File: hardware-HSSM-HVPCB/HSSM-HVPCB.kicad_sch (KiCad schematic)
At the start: 30 parts, among them J1 2086-1103, J2 2601-1110, K1 G6DN-1A-L DC12, K2 G6DN-1A-L DC12, Q1 Q_NMOS_SOT-23_IRLML6344, Q2 Q_NMOS_SOT-23_IRLML6344, U1 LNK3202D-TL, U2 CS5480-INZ

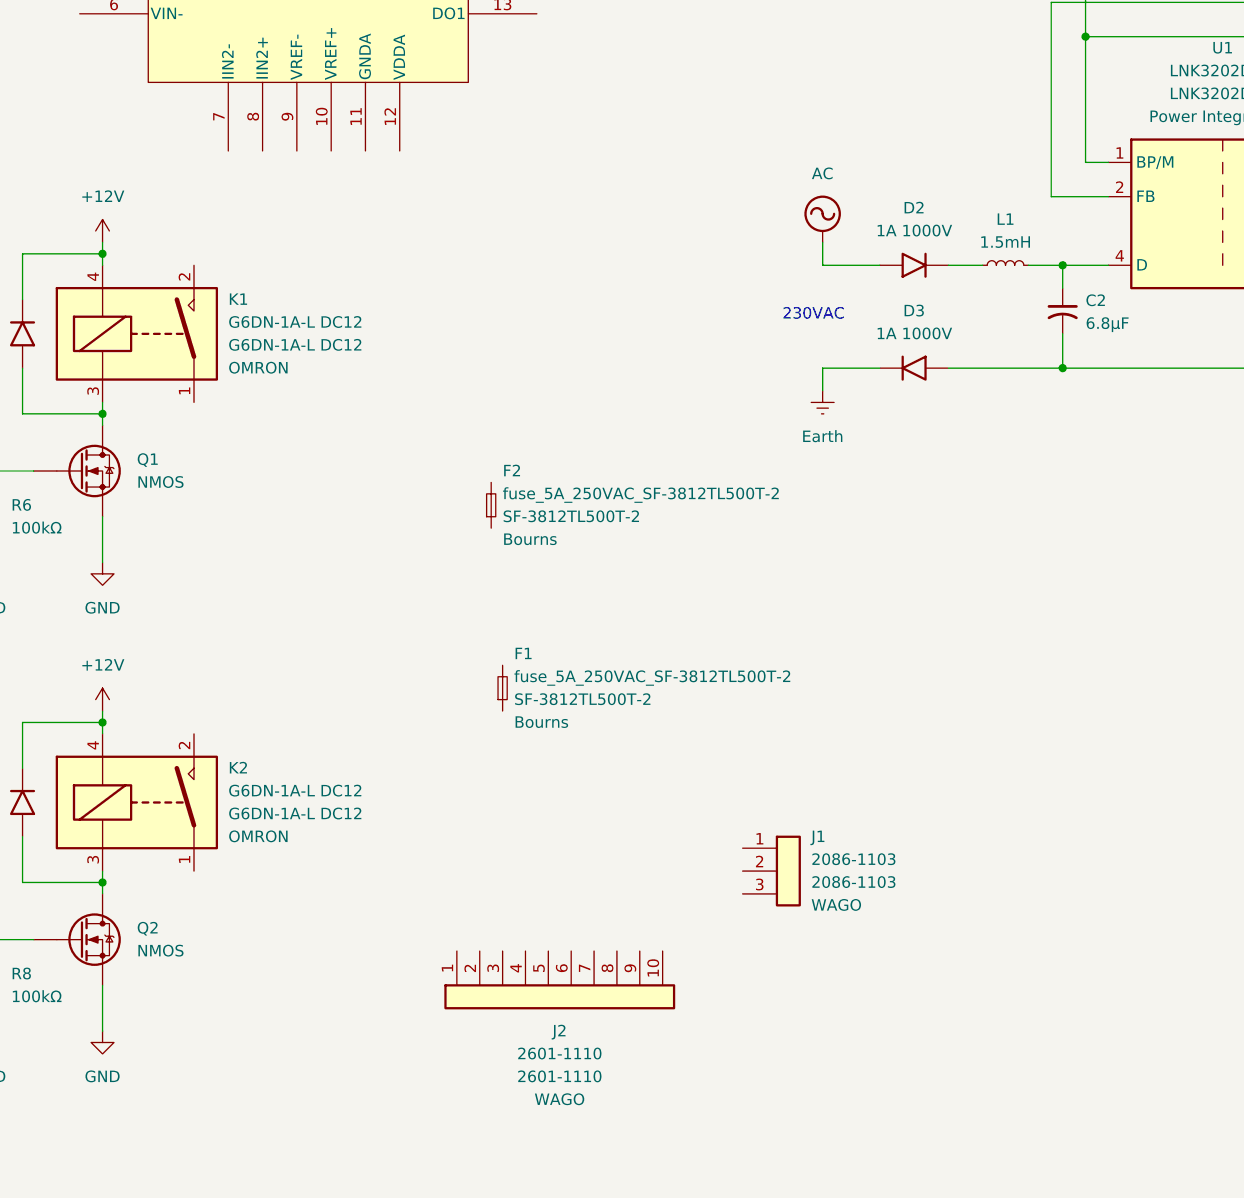
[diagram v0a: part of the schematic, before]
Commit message: [#3] SCH relay output
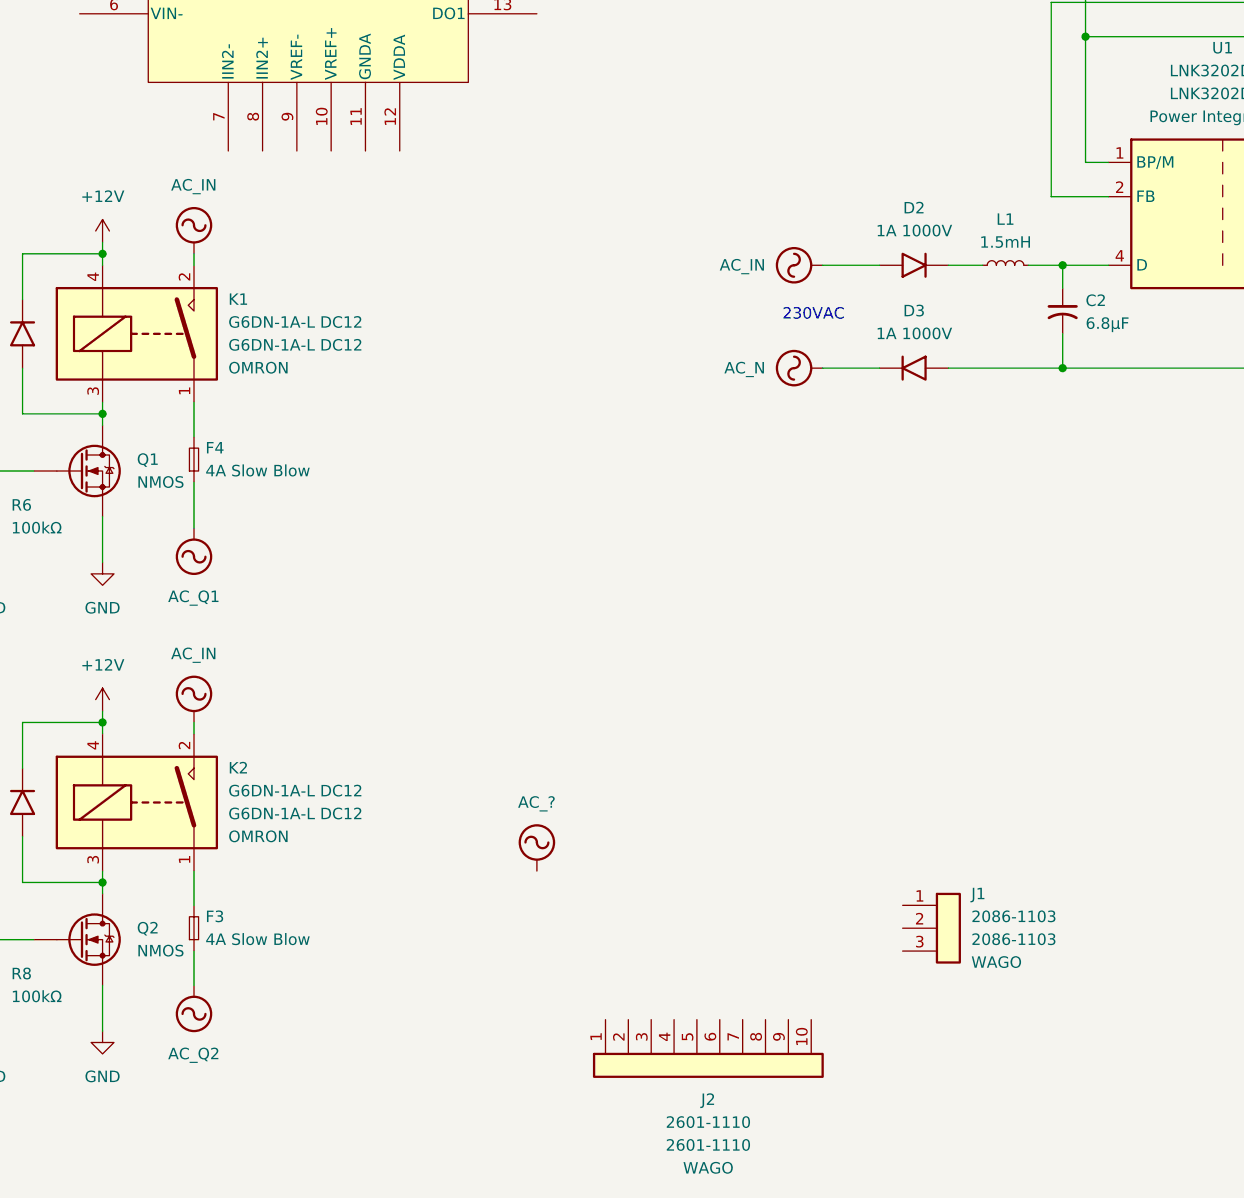
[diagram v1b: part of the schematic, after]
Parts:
- removed F1, F2: fuse_5A_250VAC_SF-3812TL500T-2, symbol HSSM-HVPCB:fuse_5A_250VAC_SF-3812TL500T-2
- added F3, F4: F_4A_SlowBlow_Holder_UMZ250_3404.2422.11, HSSM-HVPCB:F_Holder_UMZ250, symbol HSSM-HVPCB:F_4A_SlowBlow_Holder_UMZ250_3404.2422.11
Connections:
- net AC is gone; now on net AC_IN: D2.2 (A)
- net at K1.1: now also F4.2
- net AC_IN: now reaches K1.2
- net AC_IN: now also K2.2
- net at K2.1: now also F3.2
- net Earth renamed AC_N
- new net AC_Q1: F4.1
- new net AC_Q2: F3.1
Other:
- moved on the sheet: J1, J2

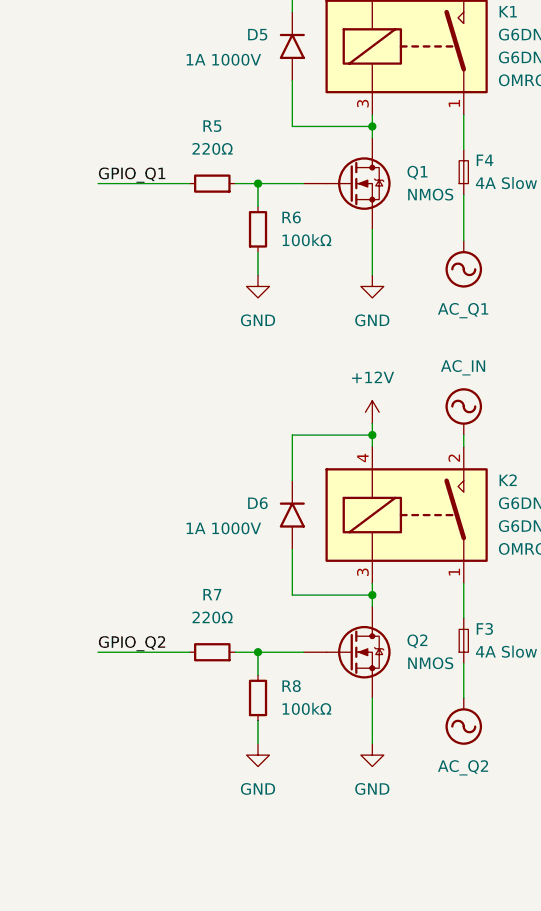
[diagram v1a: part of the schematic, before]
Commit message: [#3] SCH add relay status leds
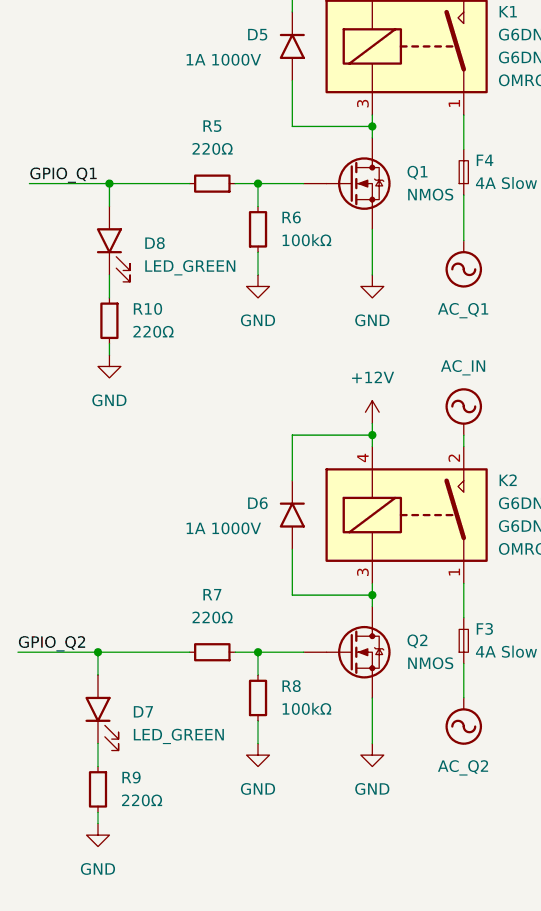
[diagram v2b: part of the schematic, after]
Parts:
- added D7, D8: LED_Green_Kingbright_APHHS1005CGCK, HSSM-HVPCB:LED_1005, symbol HSSM-HVPCB:LED_Green_Kingbright_APHHS1005CGCK
- added R10, R9: R_220R_1pct_0402_RC0402FR-07220RL, HSSM-HVPCB:R_0402, symbol HSSM-HVPCB:R_220R_1pct_0402_RC0402FR-07220RL
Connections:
- net GND: now also R10.2, R9.2
- net GPIO_Q1: now also D8.2 (A)
- net GPIO_Q2: now also D7.2 (A)
- new net: D8.1 (K), R10.1
- new net: D7.1 (K), R9.1

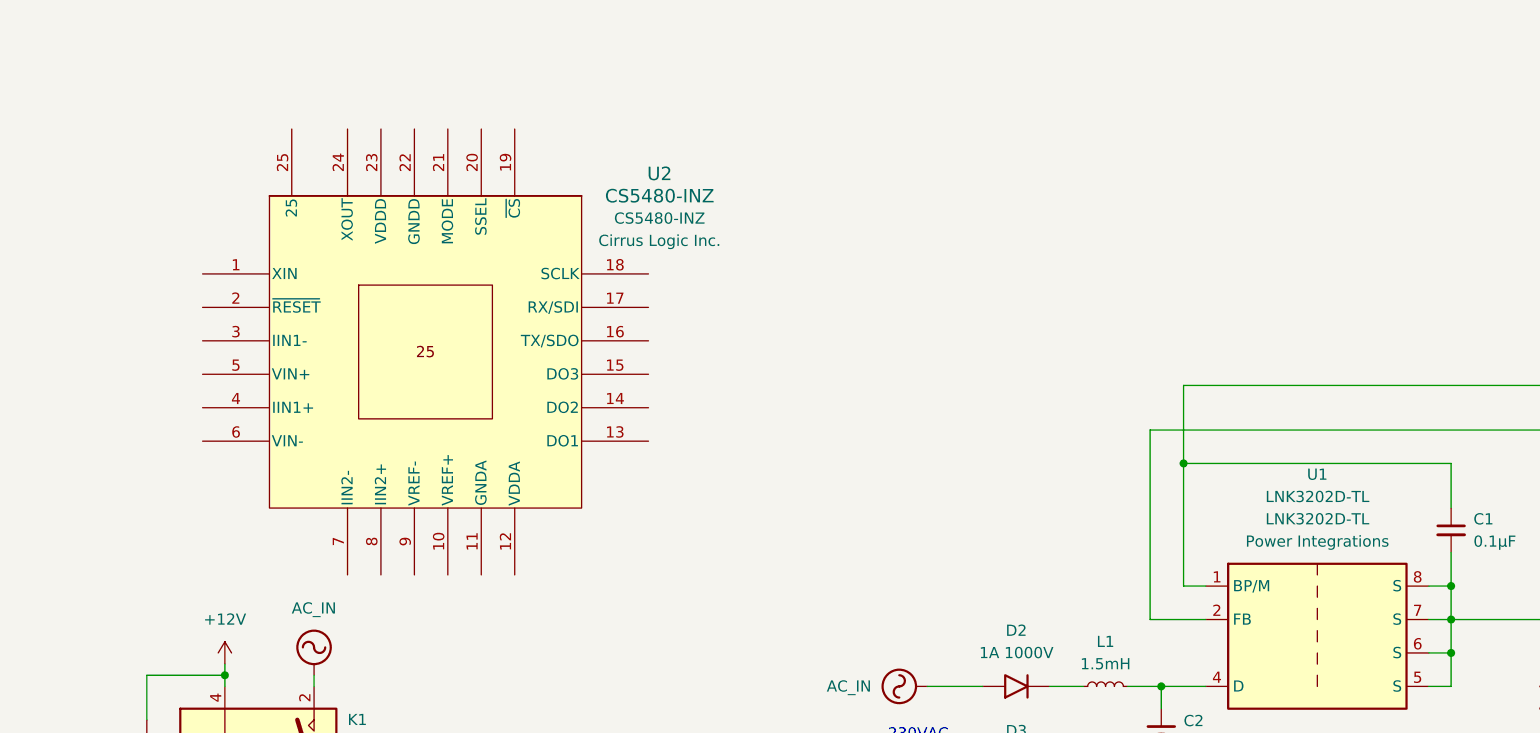
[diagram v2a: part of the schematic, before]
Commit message: [#3] Correct LNK3204D-TL symbol MPN
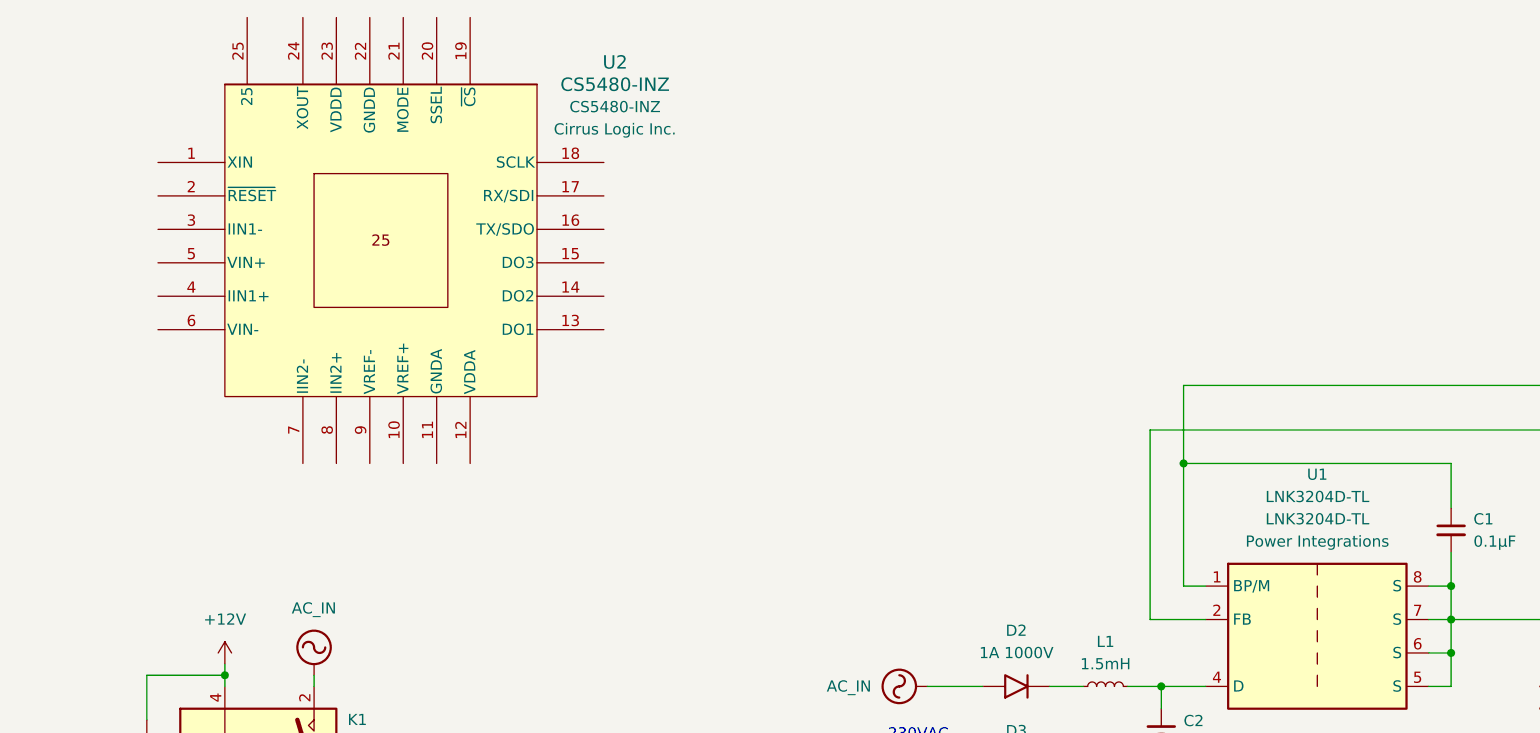
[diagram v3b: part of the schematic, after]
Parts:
- removed U1: LNK3202D-TL, symbol HSSM-HVPCB:ACDC_converter_LNK3202D-TL_power_intergrations
- added U1: LNK3204D-TL, symbol HSSM-HVPCB:ACDC_converter_LNK3204D-TL_power_intergrations
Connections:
- net at C2.1, L1.2: now also U1.4 (D)
- net at C1.2, C4.1, D1.1 (K)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: now also U1.5 (S), U1.6 (S), U1.7 (S), U1.8 (S)
- net at C1.1, R3.1: now also U1.1 (BP/M)
- net at R1.2, R2.1: now also U1.2 (FB)
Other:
- moved on the sheet: U2
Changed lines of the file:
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@@
 	(symbol
 		(lib_id "HSSM-HVPCB:power_meter_CS5480-INZ")
-		(at 76.2 55.88 0)
+		(at 71.12 43.18 0)
 		(unit 1)
 		(exclude_from_sim no)
@@
 		(fields_autoplaced yes)
 		(property "Reference" "U2"
-			(at 102.87 35.5914 0)
+			(at 97.79 22.8914 0)
 			(effects
 				(font
@@
 		)
 		(property "Value" "CS5480-INZ"
-			(at 102.87 38.1314 0)
+			(at 97.79 25.4314 0)
 			(effects
 				(font
@@
 		)
 		(property "Footprint" "CIR-QFN-24"
-			(at 73.406 55.372 0)
+			(at 68.326 42.672 0)
 			(effects
 				(font
@@
 		)
 		(property "Datasheet" "https://d3uzseaevmutz1.cloudfront.net/pubs/proDatasheet/CS5480_F3.pdf"
-			(at 73.406 55.372 0)
+			(at 68.326 42.672 0)
 			(effects
 				(font
@@
 		)
 		(property "Description" "IC ENERGY METER 3-CH 24QFN"
-			(at 73.406 55.372 0)
+			(at 68.326 42.672 0)
 			(effects
 				(font
@@
 		)
 		(property "MPN" "CS5480-INZ"
-			(at 102.87 40.6714 0)
+			(at 97.79 27.9714 0)
 			(effects
 				(font
@@
 		)
 		(property "Manufacturer" "Cirrus Logic Inc."
-			(at 102.87 43.2114 0)
+			(at 97.79 30.5114 0)
 			(effects
 				(font
@@
 	)
 	(symbol
-		(lib_id "power:AC")
-		(at 101.6 161.29 0)
+		(lib_id "HSSM-HVPCB:ACDC_converter_LNK3204D-TL_power_intergrations")
+		(at 177.8 87.63 0)
 		(unit 1)
 		(exclude_from_sim no)
@@
 		(dnp no)
 		(fields_autoplaced yes)
-		(property "Reference" "#PWR011"
-			(at 101.6 163.83 0)
+		(property "Reference" "U1"
+			(at 177.8 69.85 0)
 			(effects
 				(font
 					(size 1.27 1.27)
 				)
-				(hide yes)
 			)
 		)
-		(property "Value" "AC_?"
-			(at 101.6 153.67 0)
+		(property "Value" "LNK3204D-TL"
+			(at 177.8 72.39 0)
 			(effects
 				(font
@@
 		)
 		(property "Footprint" ""
-			(at 101.6 161.29 0)
+			(at 177.8 97.79 0)
 			(effects
 				(font
@@
 			)
 		)
-		(property "Datasheet" ""
-			(at 101.6 161.29 0)
+		(property "Datasheet" "https://www.mouser.pl/datasheet/2/328/linkswitch_tn2_family_datasheet-3043282.pdf"
+			(at 177.165 87.63 0)
 			(effects
 				(font
@@
 			)
 		)
-		(property "Description" "Power symbol creates a global label with name \"AC\""
-			(at 101.6 161.29 0)
+		(property "Description" "Converter Offline Buck, Buck-Boost, Flyback Topology 66kHz SO-8C"
+			(at 177.8 87.63 0)
 			(effects
 				(font
@@
 			)
 		)
+		(property "MPN" "LNK3204D-TL"
+			(at 177.8 74.93 0)
+			(effects
+				(font
+					(size 1.27 1.27)
+				)
+			)
+		)
+		(property "Manufacturer" "Power Integrations"
+			(at 177.8 77.47 0)
+			(effects
+				(font
+					(size 1.27 1.27)
+				)
+			)
+		)
+		(pin "4"
+		)
+		(pin "2"
+		)
+		(pin "7"
+		)
+		(pin "8"
+		)
+		(pin "6"
+		)
 		(pin "1"
 		)
+		(pin "5"
+		)
 		(instances
-			(project "HSSM-HVPCB"
+			(project ""
 				(path "/e1056638-7c6b-48e4-9e2e-c0f7b783eee5"
-					(reference "#PWR011")
+					(reference "U1")
 					(unit 1)
 				)
@@
 	)
 	(symbol
-		(lib_id "HSSM-HVPCB:ACDC_converter_LNK3202D-TL_power_intergrations")
-		(at 177.8 87.63 0)
+		(lib_id "power:AC")
+		(at 101.6 161.29 0)
 		(unit 1)
 		(exclude_from_sim no)
@@
 		(dnp no)
 		(fields_autoplaced yes)
-		(property "Reference" "U1"
-			(at 177.8 69.85 0)
+		(property "Reference" "#PWR011"
+			(at 101.6 163.83 0)
 			(effects
 				(font
 					(size 1.27 1.27)
 				)
+				(hide yes)
 			)
 		)
-		(property "Value" "LNK3202D-TL"
-			(at 177.8 72.39 0)
+		(property "Value" "AC_?"
+			(at 101.6 153.67 0)
 			(effects
 				(font
@@
 		)
 		(property "Footprint" ""
-			(at 177.8 97.79 0)
+			(at 101.6 161.29 0)
 			(effects
 				(font
@@
 			)
 		)
-		(property "Datasheet" "https://www.mouser.pl/datasheet/2/328/linkswitch_tn2_family_datasheet-3043282.pdf"
-			(at 177.165 87.63 0)
+		(property "Datasheet" ""
+			(at 101.6 161.29 0)
 			(effects
 				(font
@@
 			)
 		)
-		(property "Description" "Converter Offline Buck, Buck-Boost, Flyback Topology 66kHz SO-8C"
-			(at 177.8 87.63 0)
+		(property "Description" "Power symbol creates a global label with name \"AC\""
+			(at 101.6 161.29 0)
 			(effects
 				(font
@@
 			)
 		)
-		(property "MPN" "LNK3202D-TL"
-			(at 177.8 74.93 0)
-			(effects
-				(font
-					(size 1.27 1.27)
-				)
-			)
-		)
-		(property "Manufacturer" "Power Integrations"
-			(at 177.8 77.47 0)
-			(effects
-				(font
-					(size 1.27 1.27)
-				)
-			)
-		)
-		(pin "5"
-		)
-		(pin "2"
-		)
-		(pin "8"
-		)
-		(pin "6"
-		)
-		(pin "7"
-		)
 		(pin "1"
 		)
-		(pin "4"
-		)
 		(instances
-			(project ""
+			(project "HSSM-HVPCB"
 				(path "/e1056638-7c6b-48e4-9e2e-c0f7b783eee5"
-					(reference "U1")
+					(reference "#PWR011")
 					(unit 1)
 				)

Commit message: [#3] Add S1 and S2 switch circuit
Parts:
- added C5, C6: C_1uF_10pct_16V_0603_GCM188R71C105KA64D, HSSM-HVPCB:C_0603, symbol HSSM-HVPCB:C_1uF_10pct_16V_0603_GCM188R71C105KA64D
- added R11, R12, R14, R15: R_200k_0.1pct_1206_VT1206BRD07200KL, HSSM-HVPCB:R_1206, symbol HSSM-HVPCB:R_200k_0.1pct_1206_VT1206BRD07200KL
- added R13, R16: R_10k_1pct_0402_RC0402FR-0710KL, HSSM-HVPCB:R_0402, symbol HSSM-HVPCB:R_10k_1pct_0402_RC0402FR-0710KL
- added U3, U4: LTV-354T, HSSM-HVPCB:U_SOP4, symbol HSSM-HVPCB:U_Optocoupler_LTV-354T
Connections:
- net AC_N: now also U3.2 (K), U4.2 (K)
- net GND: now also C5.1, C6.1, U3.3 (R), U4.3 (R)
- new net: R15.2, U4.1 (A)
- new net: R11.1, R12.2
- new net: R11.2, U3.1 (A)
- new net: R14.2, R15.1
- new net +3V3: R13.2, R16.2
- new net AC_S1: R12.1
- new net AC_S2: R14.1
- new net GPIO_S1: C5.2, R13.1, U3.4 (R)
- new net GPIO_S2: C6.2, R16.1, U4.4 (R)
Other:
- note added: "230VAC -> 12VDC"
- note added: "Output 1 and output 2 relays control"
- note added: "Switch 1 and switch 2 input circuitry"
- title: (none) -> HSSM-HVPCB
- moved on the sheet: C1, C2, C3, C4, D1, D2, D3, D4, D5, D6, D7, D8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
